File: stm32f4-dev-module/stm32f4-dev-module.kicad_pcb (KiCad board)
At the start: 4 copper layers, 58.8 x 35.5 mm, 56 parts, among them J1 SWD, J10 Screw_Terminal_01x03, J11 Conn_02x10_Odd_Even, J3 I2C1, J4 SPI1, J5 5V_IN, J6 OLED, J7 USB_C_Receptacle_USB2.0_16P, J8 USART3, J9 PWM, SW1 BOOT0, SW5 BTN_UTIL, SW6 BTN_UTIL, SW7 BTN_NRST, U1 STM32F405RGT6, U2 USBLC6-2SC6, U3 SN65HVD230, U4 AP2112K-3.3, Y1 25MHz

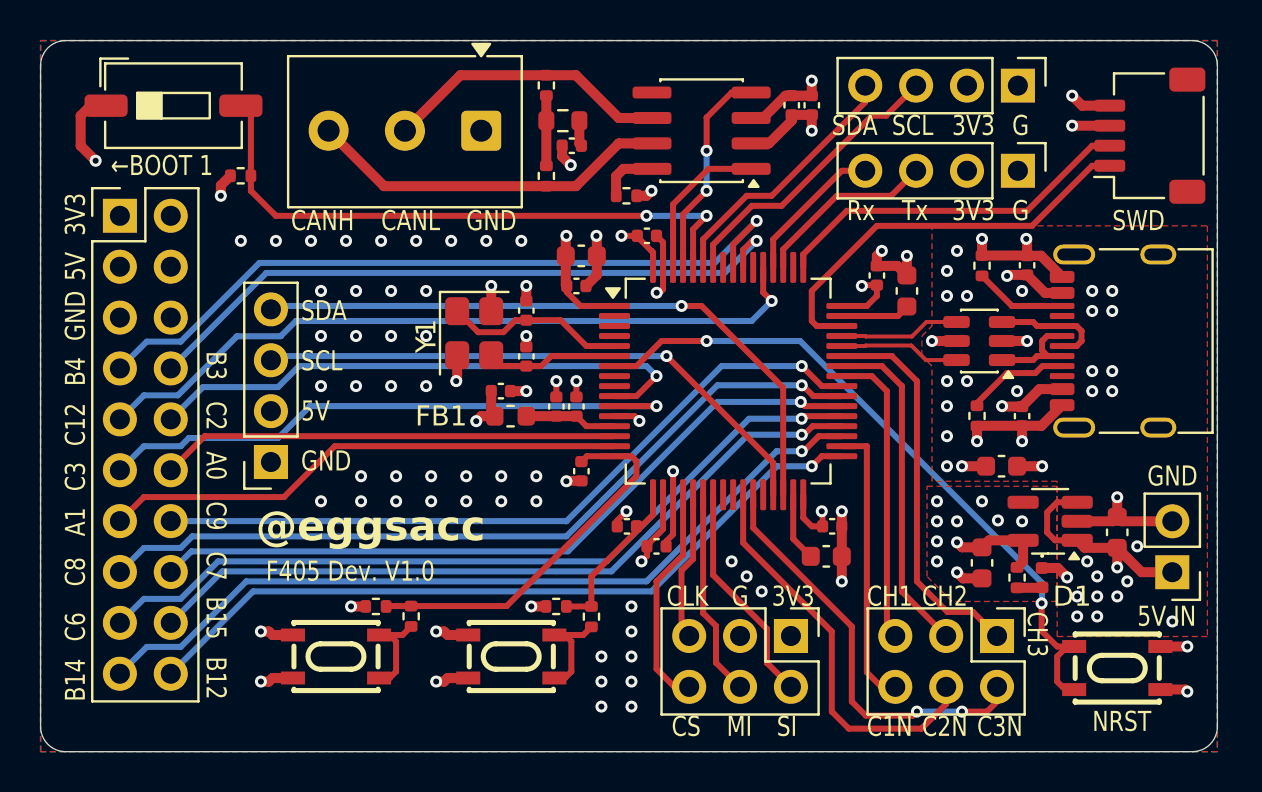
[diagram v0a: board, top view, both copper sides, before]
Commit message: Dev. module V1.1: added pull up resistors to i2c lines.
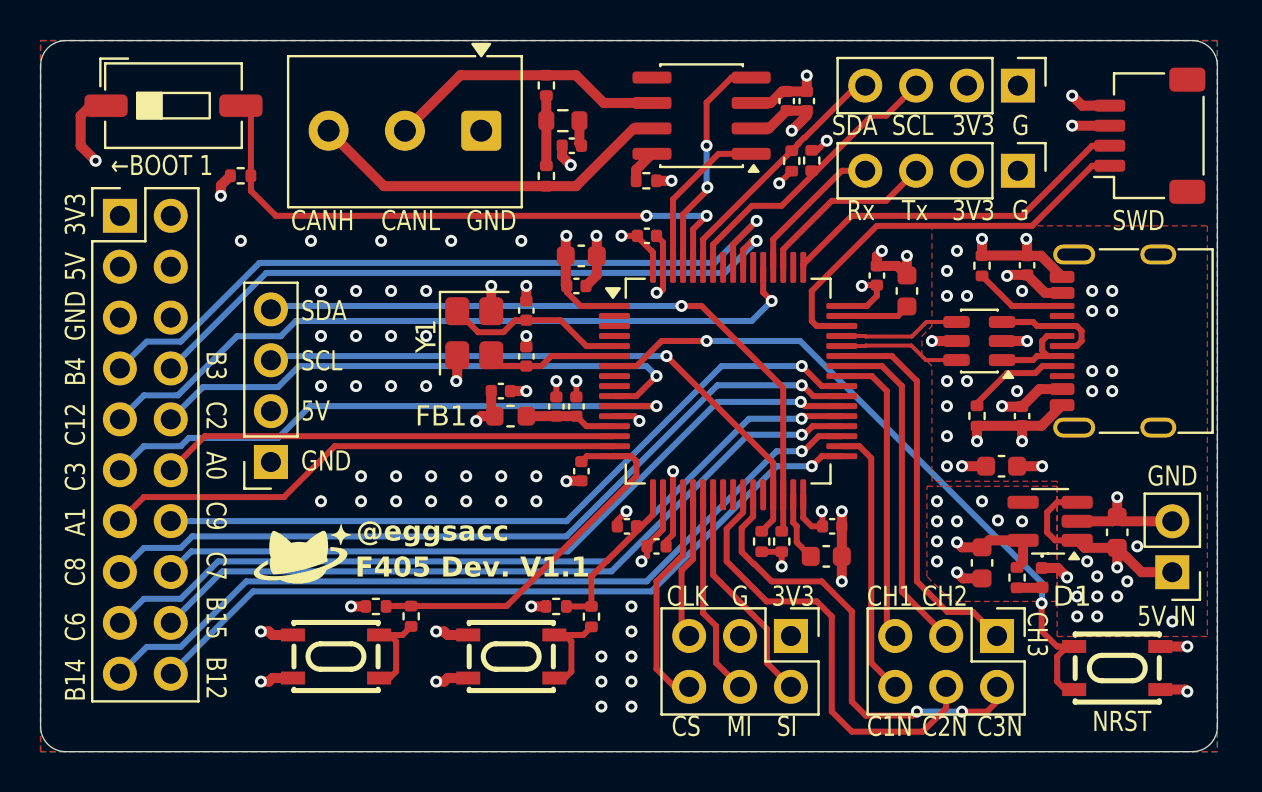
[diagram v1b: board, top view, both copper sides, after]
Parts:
- added G***: LOGO, LOGO, F.Cu at (125.0, 116.0)
- added R13: 10k, Resistor_SMD:R_0402_1005Metric, F.Cu at (149.5, 96.3)
- added R14: 10k, Resistor_SMD:R_0402_1005Metric, F.Cu at (150.5, 96.2)
- added R15: 10k, Resistor_SMD:R_0402_1005Metric, F.Cu at (148.0, 115.3)
- added R16: 10k, Resistor_SMD:R_0402_1005Metric, F.Cu at (149.0, 115.3)
- moved R3 1.24 mm to (142.2, 97.2)
- moved U3 0.75 mm to (145.0, 94.0)
- moved C16 0.33 mm to (149.2, 93.3)
- moved C17 0.33 mm to (150.2, 93.3)
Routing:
- net +3.3V: track 37.4 -> 40.5 mm, vias 20 -> 23
- net TIM1_CH2N: track 20.1 -> 22.5 mm
- net I2C2_SCL: track 29.0 -> 31.0 mm
- net TIM1_CH3N: track 20.2 -> 22.2 mm
- net I2C2_SDA: track 32.7 -> 34.5 mm
- net Net-(U3-Rs): track 2.93 -> 1.67 mm
- net CAN1_Rx: track 10.7 -> 11.5 mm
- net TIM1_CH1N: track 14.3 -> 13.6 mm
- net GND: track 68.8 -> 68.6 mm, vias 82 -> 75
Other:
- board text added: "F405 Dev. V1.1"
- board text removed: "F405 Dev. V1.0"
